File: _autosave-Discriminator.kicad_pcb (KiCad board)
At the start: 4 copper layers, 35.8 x 27.5 mm, 29 parts, among them J1 Conn_01x05_Socket, J3 Conn_Coaxial, U1 PSA4-5043+, U2 PGA-103+

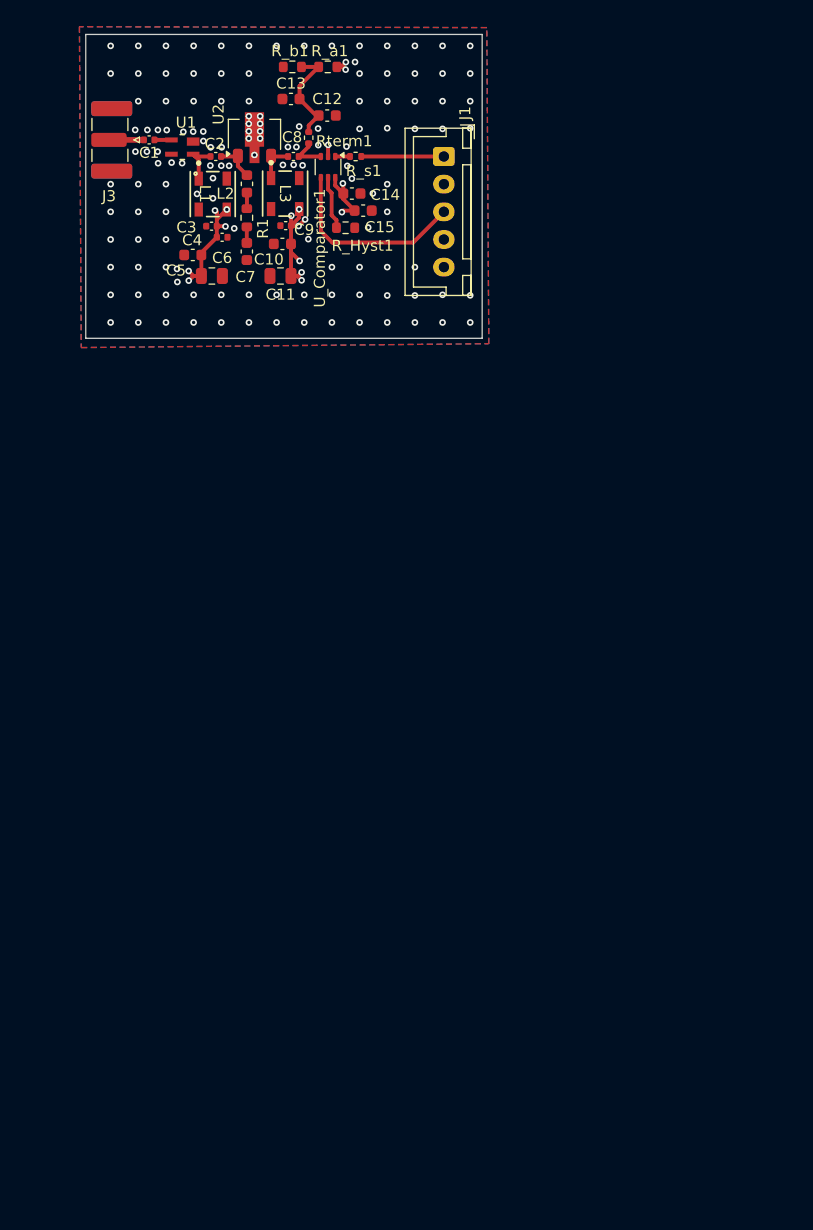
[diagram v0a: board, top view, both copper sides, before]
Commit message: added mcu section, added test points to CTD
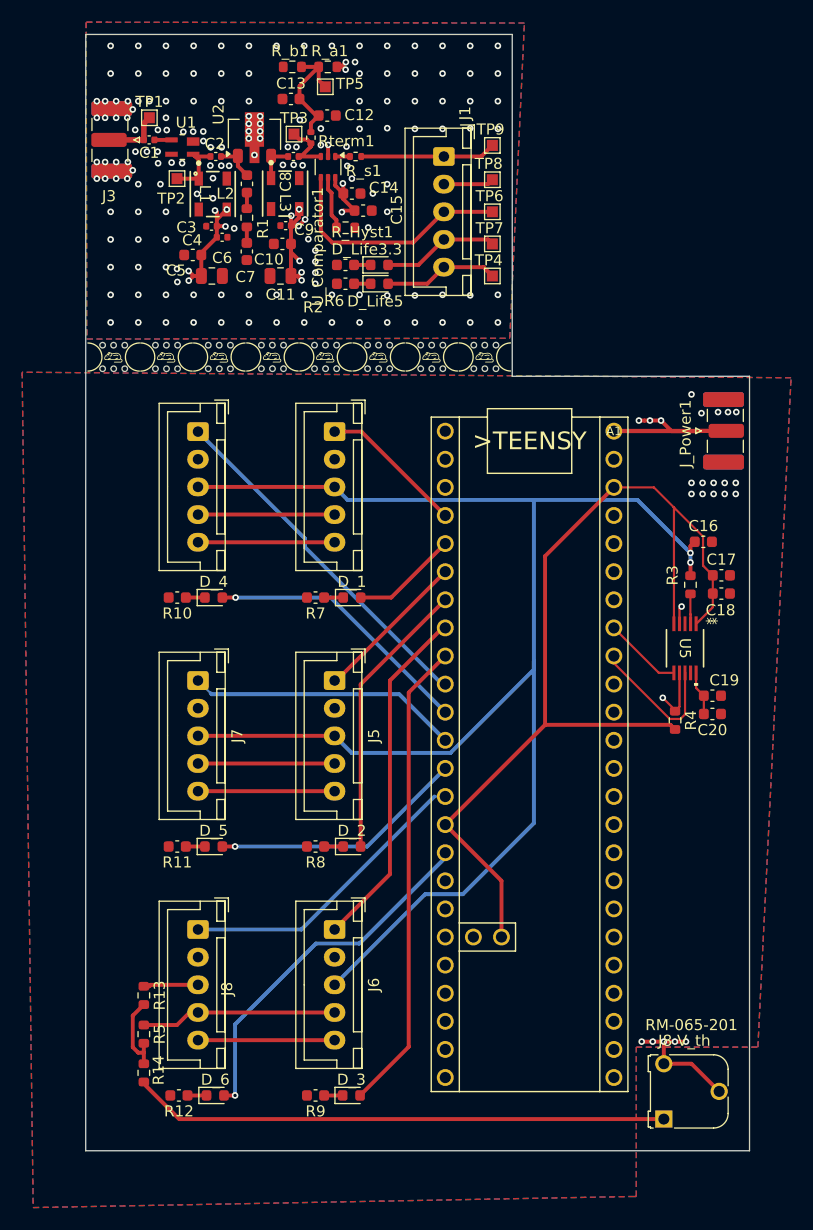
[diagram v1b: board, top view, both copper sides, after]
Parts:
- added A1: TEENSY_4.1, TEENSY_4.1:TEENSY_LONG_EXT, F.Cu at (168.0, 62.3)
- added C16: 0.1uf, Capacitor_SMD:C_0603_1608Metric, F.Cu at (176.1, 72.3)
- added C17: 1uf, Capacitor_SMD:C_0603_1608Metric, F.Cu at (177.7, 75.4)
- added C18: 0.1uf, Capacitor_SMD:C_0603_1608Metric, F.Cu at (177.7, 77.0)
- added C19: 1uf, Capacitor_SMD:C_0603_1608Metric, F.Cu at (176.9, 86.2)
- added C20: 0.1uf, Capacitor_SMD:C_0603_1608Metric, F.Cu at (176.9, 87.9)
- added D_1: LED, LED_SMD:LED_0603_1608Metric, F.Cu at (144.3, 77.4)
- added D_2: LED, LED_SMD:LED_0603_1608Metric, F.Cu at (144.3, 99.9)
- added D_3: LED, LED_SMD:LED_0603_1608Metric, F.Cu at (144.3, 122.4)
- added D_4: LED, LED_SMD:LED_0603_1608Metric, F.Cu at (131.8, 77.4)
- added D_5: LED, LED_SMD:LED_0603_1608Metric, F.Cu at (131.8, 99.9)
- added D_6: LED, LED_SMD:LED_0603_1608Metric, F.Cu at (132.0, 122.4)
- added D_Life3.3: LED, LED_SMD:LED_0603_1608Metric, F.Cu at (146.8, 47.3)
- added D_Life5: LED, LED_SMD:LED_0603_1608Metric, F.Cu at (146.8, 49.0)
- added J2: Conn_01x05_Socket, Connector_JST:JST_XH_B5B-XH-A_1x05_P2.50mm_Vertical, F.Cu at (142.7, 62.4)
- added J4: Conn_01x05_Socket, Connector_JST:JST_XH_B5B-XH-A_1x05_P2.50mm_Vertical, F.Cu at (130.4, 62.4)
- added J5: Conn_01x05_Socket, Connector_JST:JST_XH_B5B-XH-A_1x05_P2.50mm_Vertical, F.Cu at (142.7, 84.9)
- added J6: Conn_01x05_Socket, Connector_JST:JST_XH_B5B-XH-A_1x05_P2.50mm_Vertical, F.Cu at (142.7, 107.4)
- added J7: Conn_01x05_Socket, Connector_JST:JST_XH_B5B-XH-A_1x05_P2.50mm_Vertical, F.Cu at (130.4, 84.9)
- added J8: Conn_01x05_Socket, Connector_JST:JST_XH_B5B-XH-A_1x05_P2.50mm_Vertical, F.Cu at (130.4, 107.4)
- added J_Power1: Conn_Coaxial, Connector_Coaxial:SMA_Samtec_SMA-J-P-H-ST-EM1_EdgeMount, F.Cu at (178.1, 62.3)
- added R10: 2k, Capacitor_SMD:C_0603_1608Metric, F.Cu at (128.5, 77.4)
- added R11: 2k, Capacitor_SMD:C_0603_1608Metric, F.Cu at (128.5, 99.9)
- added R12: 2k, Capacitor_SMD:C_0603_1608Metric, F.Cu at (128.7, 122.4)
- added R13: 1k, Resistor_SMD:R_0603_1608Metric, F.Cu at (125.5, 113.3)
- added R14: 1k, Resistor_SMD:R_0603_1608Metric, F.Cu at (125.5, 120.3)
- added R2: 2k, Capacitor_SMD:C_0603_1608Metric, F.Cu at (143.7, 47.3)
- added R3: 1k, Resistor_SMD:R_0603_1608Metric, F.Cu at (174.9, 76.2)
- added R4: 4.7k, Resistor_SMD:R_0603_1608Metric, F.Cu at (173.5, 88.5)
- added R5: 5.6k, Resistor_SMD:R_0603_1608Metric, F.Cu at (125.5, 116.8)
- added R6: 2k, Capacitor_SMD:C_0603_1608Metric, F.Cu at (143.7, 49.0)
- added R7: 2k, Capacitor_SMD:C_0603_1608Metric, F.Cu at (141.0, 77.4)
- added R8: 2k, Capacitor_SMD:C_0603_1608Metric, F.Cu at (141.0, 99.9)
- added R9: 2k, Capacitor_SMD:C_0603_1608Metric, F.Cu at (141.0, 122.4)
- added RM-065-201: 200ohms, Potentiometer_THT:Potentiometer_Runtron_RM-065_Vertical, F.Cu at (172.5, 124.5)
- added TP1: TestPoint, TestPoint:TestPoint_Pad_1.0x1.0mm, F.Cu at (126.0, 34.0)
- added TP2: TestPoint, TestPoint:TestPoint_Pad_1.0x1.0mm, F.Cu at (128.5, 39.5)
- added TP3: TestPoint, TestPoint:TestPoint_Pad_1.0x1.0mm, F.Cu at (139.1, 35.5)
- added TP4: TestPoint, TestPoint:TestPoint_Pad_1.0x1.0mm, F.Cu at (157.0, 48.3)
- added TP5: TestPoint, TestPoint:TestPoint_Pad_1.0x1.0mm, F.Cu at (141.9, 31.2)
- added TP6: TestPoint, TestPoint:TestPoint_Pad_1.0x1.0mm, F.Cu at (157.0, 42.5)
- added TP7: TestPoint, TestPoint:TestPoint_Pad_1.0x1.0mm, F.Cu at (157.0, 45.4)
- added TP8: TestPoint, TestPoint:TestPoint_Pad_1.0x1.0mm, F.Cu at (157.0, 39.6)
- added TP9: TestPoint, TestPoint:TestPoint_Pad_1.0x1.0mm, F.Cu at (157.0, 36.5)
- added U5: DAC60501-0x49, DAC60501ZDGSR:DGS10_TEX, F.Cu at (174.4, 82.0)
- added mouse-bite-2.54mm-4.66mm: VAL**, mouse-bite.pretty-main:mouse-bite-2.54mm-4.66mm, F.Cu at (151.5, 55.6)
- added mouse-bite-2.54mm-4.66mm: VAL**, mouse-bite.pretty-main:mouse-bite-2.54mm-4.66mm, F.Cu at (132.3, 55.6)
- added mouse-bite-2.54mm-4.66mm: VAL**, mouse-bite.pretty-main:mouse-bite-2.54mm-4.66mm, F.Cu at (137.1, 55.6)
- added mouse-bite-2.54mm-4.66mm: VAL**, mouse-bite.pretty-main:mouse-bite-2.54mm-4.66mm, F.Cu at (141.9, 55.6)
- added mouse-bite-2.54mm-4.66mm: VAL**, mouse-bite.pretty-main:mouse-bite-2.54mm-4.66mm, F.Cu at (156.3, 55.6)
- added mouse-bite-2.54mm-4.66mm: VAL**, mouse-bite.pretty-main:mouse-bite-2.54mm-4.66mm, F.Cu at (146.7, 55.6)
- added mouse-bite-2.54mm-4.66mm: VAL**, mouse-bite.pretty-main:mouse-bite-2.54mm-4.66mm, F.Cu at (127.5, 55.6)
- added mouse-bite-2.54mm-4.66mm: VAL**, mouse-bite.pretty-main:mouse-bite-2.54mm-4.66mm, F.Cu at (122.8, 55.6)
- moved Rterm1 0.20 mm to (140.6, 35.8)
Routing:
- net +3.3VA: track 0.00 -> 194.6 mm
- net +5VA: track 0.00 -> 162.5 mm, vias 0 -> 3
- net /V_r: track 0.00 -> 138.4 mm, vias 0 -> 2
- net Net-(R14-Pad1): track 0.00 -> 48.5 mm
- net Net-(D_3-A): track 0.00 -> 42.9 mm
- net Net-(A1-A10): track 0.00 -> 33.1 mm, vias 0 -> 1
- net /4: track 0.00 -> 32.0 mm
- net /3: track 0.00 -> 31.5 mm
- net /6: track 0.00 -> 27.3 mm
- net Net-(D_2-A): track 0.00 -> 25.5 mm
- net /5: track 0.00 -> 24.6 mm
- net Net-(D_4-A): track 0.00 -> 24.4 mm, vias 0 -> 1
- net Net-(A1-(SDO)D11): track 0.00 -> 23.1 mm, vias 0 -> 1
- net /2: track 0.00 -> 14.1 mm
- net GNDA: track 0.00 -> 13.7 mm, vias 0 -> 21
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- added copper zone on B.Cu, net GNDA
- added copper zone on F.Cu, net GNDA
- added copper zone on In1.Cu, net GNDA
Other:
- board size 35.8 x 27.5 mm -> 60 x 100.9 mm
- board text added: "J8 V_th"

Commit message: Misc changes
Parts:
- R6: value 2k -> 4.7k
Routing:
- net GNDA: vias 21 -> 19
- net GND: vias 160 -> 155
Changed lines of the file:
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@@
 		(tags "resistor")
 		(property "Reference" "R_Hyst1"
-			(at 1.505 0.4 0)
+			(at 1.765 0.4 0)
 			(layer "F.SilkS")
 			(effects
@@
 		(tags "capacitor")
 		(property "Reference" "R6"
-			(at 1.025 -1.55 0)
+			(at 0.725 -3 0)
 			(layer "F.SilkS")
 			(effects
@@
 			)
 		)
-		(property "Value" "2k"
+		(property "Value" "4.7k"
 			(at -0.025 -1.25 0)
 			(layer "F.Fab")
@@
 		(tags "LED")
 		(property "Reference" "D_Life5"
-			(at -0.3675 1.59 0)
+			(at 0.2125 2 0)
 			(layer "F.SilkS")
 			(effects
@@
 		(tags "capacitor")
 		(property "Reference" "R2"
-			(at 2.925 -3.825 0)
+			(at 0.725 -3.45 0)
 			(layer "F.SilkS")
 			(effects
@@
 	)
 	(via
-		(at 141 49)
-		(size 0.6)
-		(drill 0.3)
-		(layers "F.Cu" "B.Cu")
-		(free yes)
-		(net 4)
-	)
-	(via
 		(at 122.5 30)
 		(size 0.6)
@@
 	)
 	(via
-		(at 131.75 41.28)
-		(size 0.6)
-		(drill 0.3)
-		(layers "F.Cu" "B.Cu")
-		(free yes)
-		(net 4)
-	)
-	(via
 		(at 145.78 43.92)
 		(size 0.6)
@@
 	)
 	(via
-		(at 141 47)
-		(size 0.6)
-		(drill 0.3)
-		(layers "F.Cu" "B.Cu")
-		(free yes)
-		(net 4)
-	)
-	(via
 		(at 122.5 47.5)
 		(size 0.6)
@@
 	)
 	(via
-		(at 124.5 33.25)
-		(size 0.6)
-		(drill 0.3)
-		(layers "F.Cu" "B.Cu")
-		(net 4)
-	)
-	(via
 		(at 152.5 32.5)
 		(size 0.6)
@@
 	)
 	(via
-		(at 124.5 38.75)
-		(size 0.6)
-		(drill 0.3)
-		(layers "F.Cu" "B.Cu")
-		(net 4)
-	)
-	(via
 		(at 141 46)
 		(size 0.6)
@@
 		(start 172.5 119.5)
 		(end 172.5 117.5)
-		(width 0.355542)
+		(width 0.8)
 		(layer "F.Cu")
 		(net 17)
@@
 	)
 	(via
-		(at 175 59)
-		(size 0.6)
-		(drill 0.3)
-		(layers "F.Cu" "B.Cu")
-		(free yes)
-		(net 17)
-	)
-	(via
 		(at 178 67)
 		(size 0.6)
@@
 	)
 	(via
-		(at 175.9 60.7)
-		(size 0.6)
-		(drill 0.3)
-		(layers "F.Cu" "B.Cu")
-		(free yes)
-		(net 17)
-	)
-	(via
 		(at 178 68)
 		(size 0.6)
@@
 		(name "$teardrop_padvia$")
 		(hatch none 0.1)
-		(priority 30000)
+		(priority 30001)
 		(attr
 			(teardrop
@@
 		(polygon
 			(pts
-				(xy 124.95 36.25) (xy 124.95 35.75) (xy 123.795671 35.38403) (xy 122.349 36) (xy 123.795671 36.61597)
+				(xy 125.75 35.13) (xy 125.25 35.13) (xy 125.22 35.83) (xy 125.5 36.001) (xy 125.78 35.83)
 			)
 		)
@@
 		(name "$teardrop_padvia$")
 		(hatch none 0.1)
-		(priority 30001)
+		(priority 30000)
 		(attr
 			(teardrop
@@
 		(polygon
 			(pts
-				(xy 125.75 35.13) (xy 125.25 35.13) (xy 125.22 35.83) (xy 125.5 36.001) (xy 125.78 35.83)
+				(xy 124.95 36.25) (xy 124.95 35.75) (xy 123.795671 35.38403) (xy 122.349 36) (xy 123.795671 36.61597)
 			)
 		)
